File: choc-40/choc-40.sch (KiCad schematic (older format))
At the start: 103 parts, among them SW1 SW_Push, SW10 SW_Push, SW11 SW_Push, SW12 SW_Push, SW13 SW_Push, SW14 SW_Push, SW15 SW_Push, SW16 SW_Push, SW17 SW_Push, SW18 SW_Push, SW19 SW_Push, SW2 SW_Push, SW20 SW_Push, SW21 SW_Push, SW22 SW_Push, SW23 SW_Push, SW24 SW_Push, SW25 SW_Push, SW26 SW_Push, SW27 SW_Push, SW28 SW_Push, SW29 SW_Push, SW3 SW_Push, SW30 SW_Push, SW31 SW_Push, SW32 SW_Push, SW33 SW_Push, SW34 SW_Push, SW35 SW_Push, SW36 SW_Push, SW37 SW_Push, SW38 SW_Push, SW39 SW_Push, SW4 SW_Push, SW40 SW_Push, SW41 SW_Push, SW42 SW_Push, SW43 SW_Push, SW44 SW_Push, SW45 SW_Push, SW46 SW_Push, SW47 SW_Push, SW48 SW_Push, SW49 SW_Push, SW5 SW_Push, SW6 SW_Push, SW7 SW_Push, SW8 SW_Push, SW9 SW_Push, U2 ProMicro

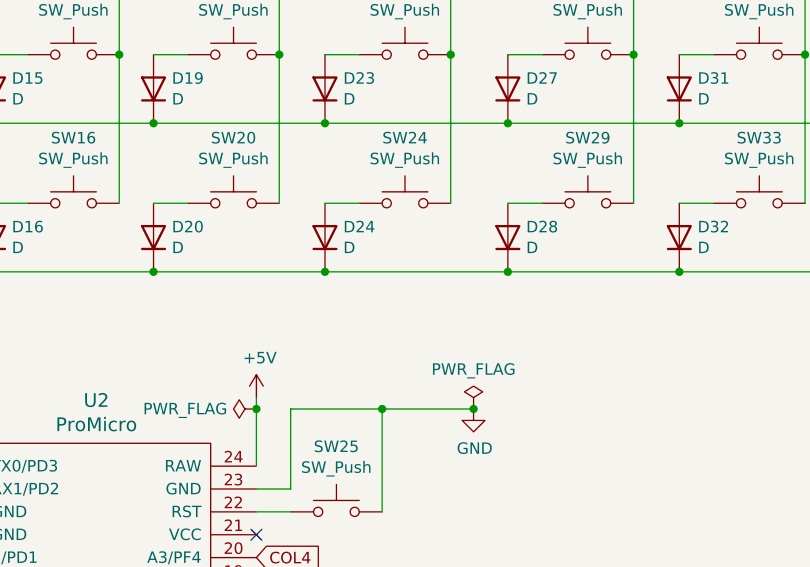
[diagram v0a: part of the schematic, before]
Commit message: adding 2u middle key option
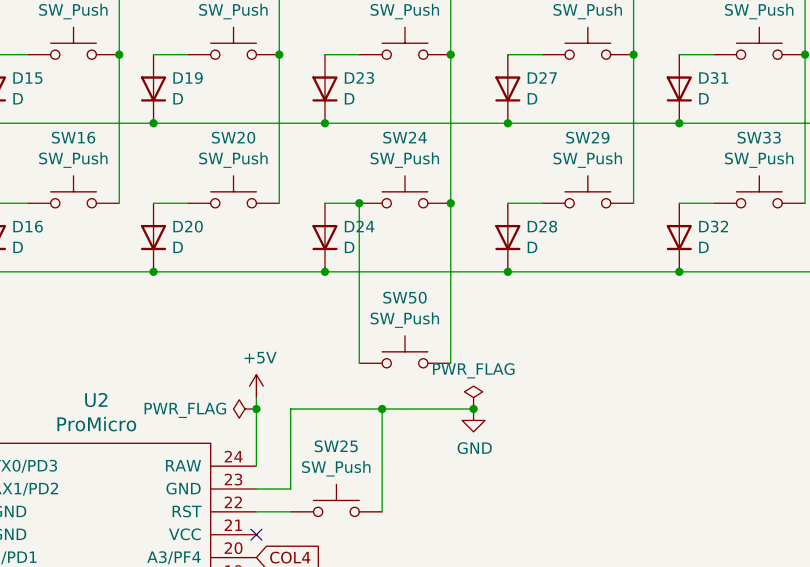
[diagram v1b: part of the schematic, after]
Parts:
- added SW50: SW_Push, Keebio-Parts:Kailh-PG1350-2u-NoLED, symbol Switch:SW_Push
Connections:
- net COL6: now also SW50.2
- net at D24.2 (A), SW24.1: now also SW50.1
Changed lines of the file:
@@
 	1    0    0    -1
 $EndComp
+$Comp
+L Switch:SW_Push SW50
+U 1 1 605A6636
+P 5350 4350
+F 0 "SW50" H 5350 4635 50  0000 C CNN
+F 1 "SW_Push" H 5350 4544 50  0000 C CNN
+F 2 "Keebio-Parts:Kailh-PG1350-2u-NoLED" H 5350 4550 50  0001 C CNN
+F 3 "~" H 5350 4550 50  0001 C CNN
+	1    5350 4350
+	1    0    0    -1
+$EndComp
+Wire Wire Line
+	5550 3650 5550 4350
+Connection ~ 5550 3650
+Wire Wire Line
+	5150 3650 5150 4350
+Connection ~ 5150 3650
 $EndSCHEMATC

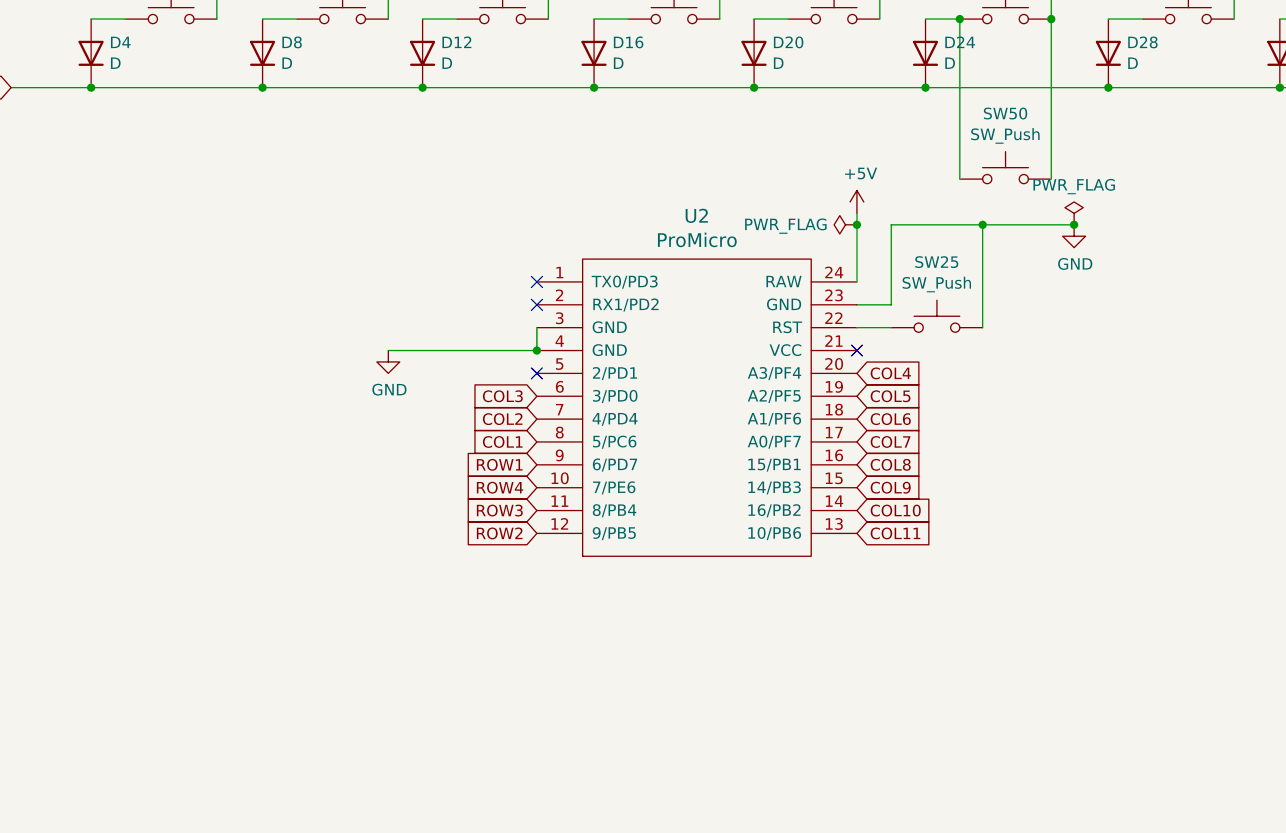
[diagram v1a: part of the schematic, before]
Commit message: adding base and plate
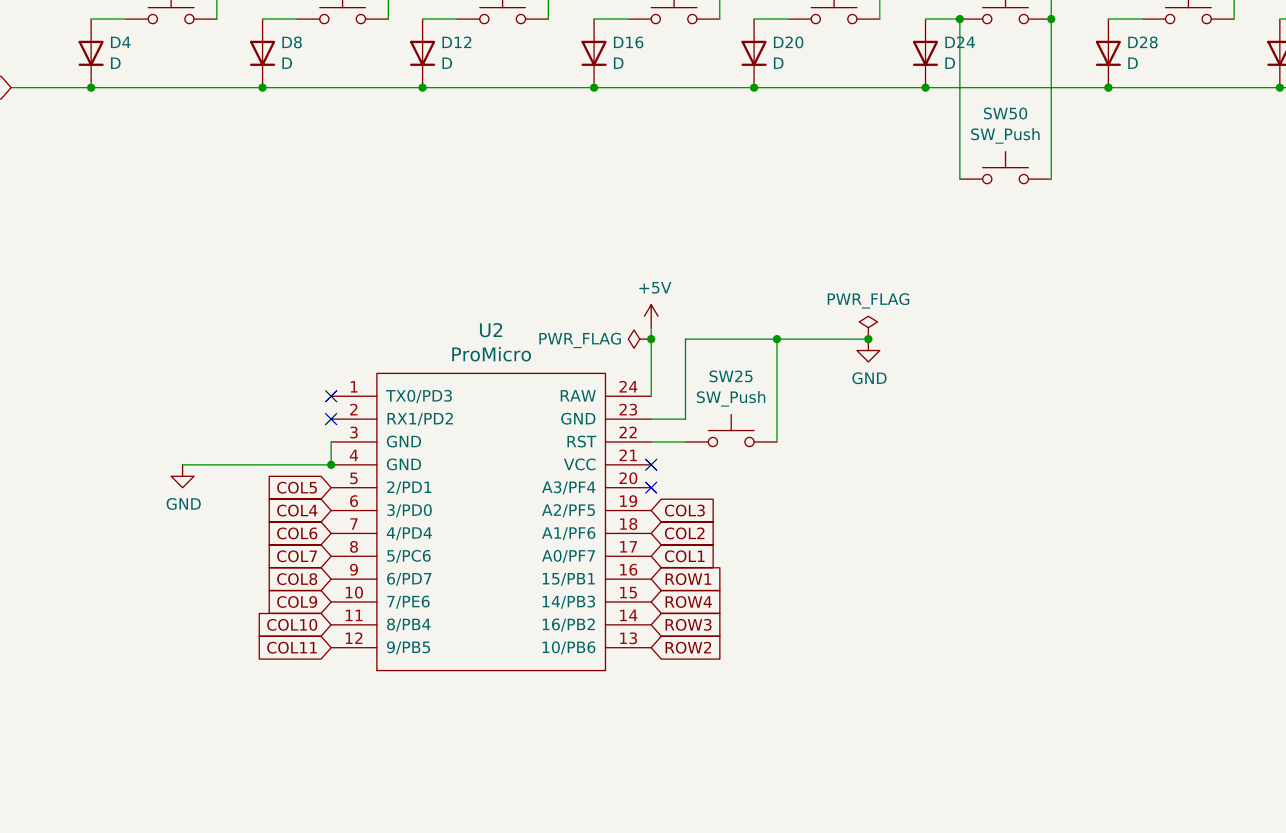
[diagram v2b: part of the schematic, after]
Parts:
- D1, D10, D11, D12, D13, D14, D15, D16, D17, D18, D19, D2, D20, D21, D22, D23, D24, D25, D26, D27, D28, D29, D3, D30, D31, D32, D33, D34, D35, D36, D37, D38, D39, D4, D40, D41, D42, D43, D44, D45, D46, D47, D48, D5, D6, D7, D8, D9: footprint Diode_THT:D_DO-35_SOD27_P10.16mm_Horizontal -> keyboard_parts:D_SOD123_axial
- U2: footprint Keebio-Parts:ArduinoProMicro -> Keebio-Parts:ArduinoProMicro-TopSide
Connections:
- net COL1: now also U2.17 (A0/PF7); no longer U2.8 (5/PC6)
- net COL10: now also U2.11 (8/PB4); no longer U2.14 (16/PB2)
- net COL11: now also U2.12 (9/PB5); no longer U2.13 (10/PB6)
- net COL2: now also U2.18 (A1/PF6); no longer U2.7 (4/PD4)
- net COL3: now also U2.19 (A2/PF5); no longer U2.6 (3/PD0)
- net COL4: now also U2.6 (3/PD0); no longer U2.20 (A3/PF4)
- net COL5: now also U2.5 (2/PD1); no longer U2.19 (A2/PF5)
- net COL6: now also U2.7 (4/PD4); no longer U2.18 (A1/PF6)
- net COL7: now also U2.8 (5/PC6); no longer U2.17 (A0/PF7)
- net COL8: now also U2.9 (6/PD7); no longer U2.16 (15/PB1)
- net COL9: now also U2.10 (7/PE6); no longer U2.15 (14/PB3)
- net ROW1: now also U2.16 (15/PB1); no longer U2.9 (6/PD7)
- net ROW2: now also U2.13 (10/PB6); no longer U2.12 (9/PB5)
- net ROW3: now also U2.14 (16/PB2); no longer U2.11 (8/PB4)
- net ROW4: now also U2.15 (14/PB3); no longer U2.10 (7/PE6)
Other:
- moved on the sheet: SW25, U2

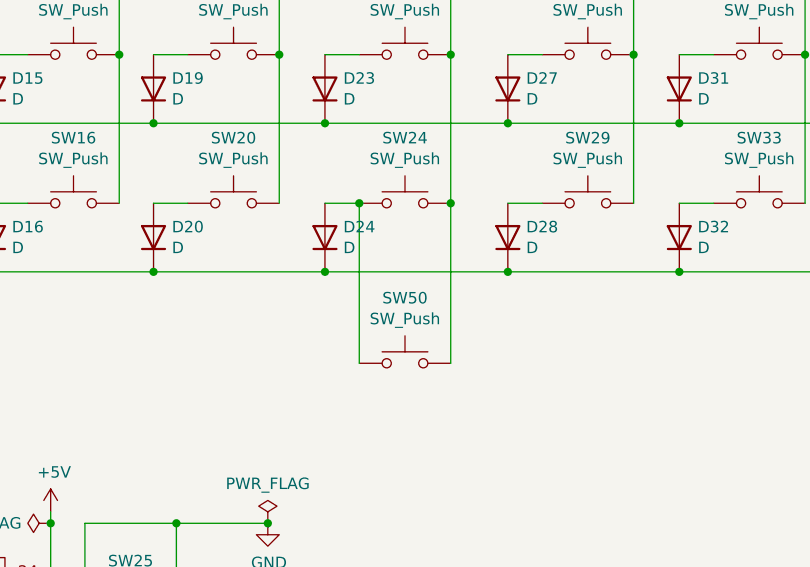
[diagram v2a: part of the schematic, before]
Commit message: updating plate to 13.8x13.8mm
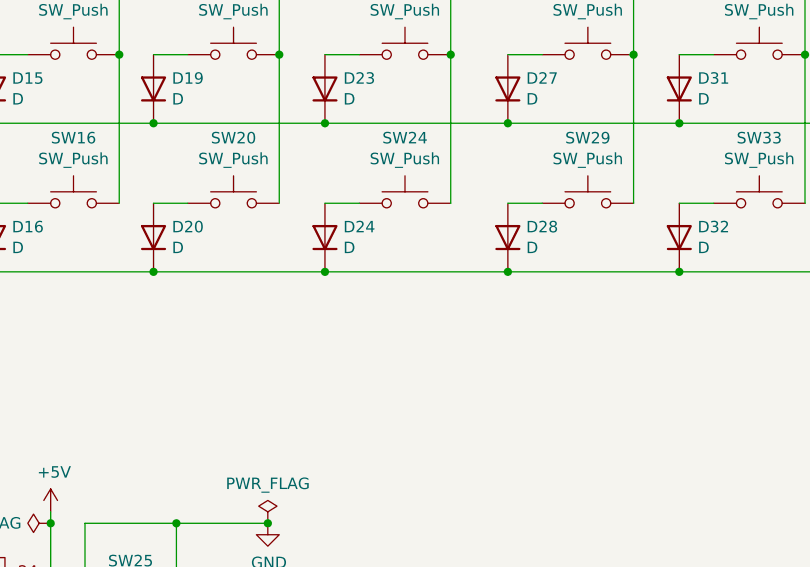
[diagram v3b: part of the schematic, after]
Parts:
- removed SW50: SW_Push, Keebio-Parts:Kailh-PG1350-2u-NoLED, symbol Switch:SW_Push
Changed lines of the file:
@@
-	1    0    0    -1
-$EndComp
-$Comp
-L Switch:SW_Push SW50
-U 1 1 605A6636
-P 5350 4350
-F 0 "SW50" H 5350 4635 50  0000 C CNN
-F 1 "SW_Push" H 5350 4544 50  0000 C CNN
-F 2 "Keebio-Parts:Kailh-PG1350-2u-NoLED" H 5350 4550 50  0001 C CNN
-F 3 "~" H 5350 4550 50  0001 C CNN
-	1    5350 4350
 	1    0    0    -1
 $EndComp
 Wire Wire Line
-	5550 3650 5550 4350
-Connection ~ 5550 3650
-Wire Wire Line
-	5150 3650 5150 4350
-Connection ~ 5150 3650
-Wire Wire Line
 	3800 5300 3800 5050
